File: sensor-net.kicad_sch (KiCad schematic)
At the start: 11 parts

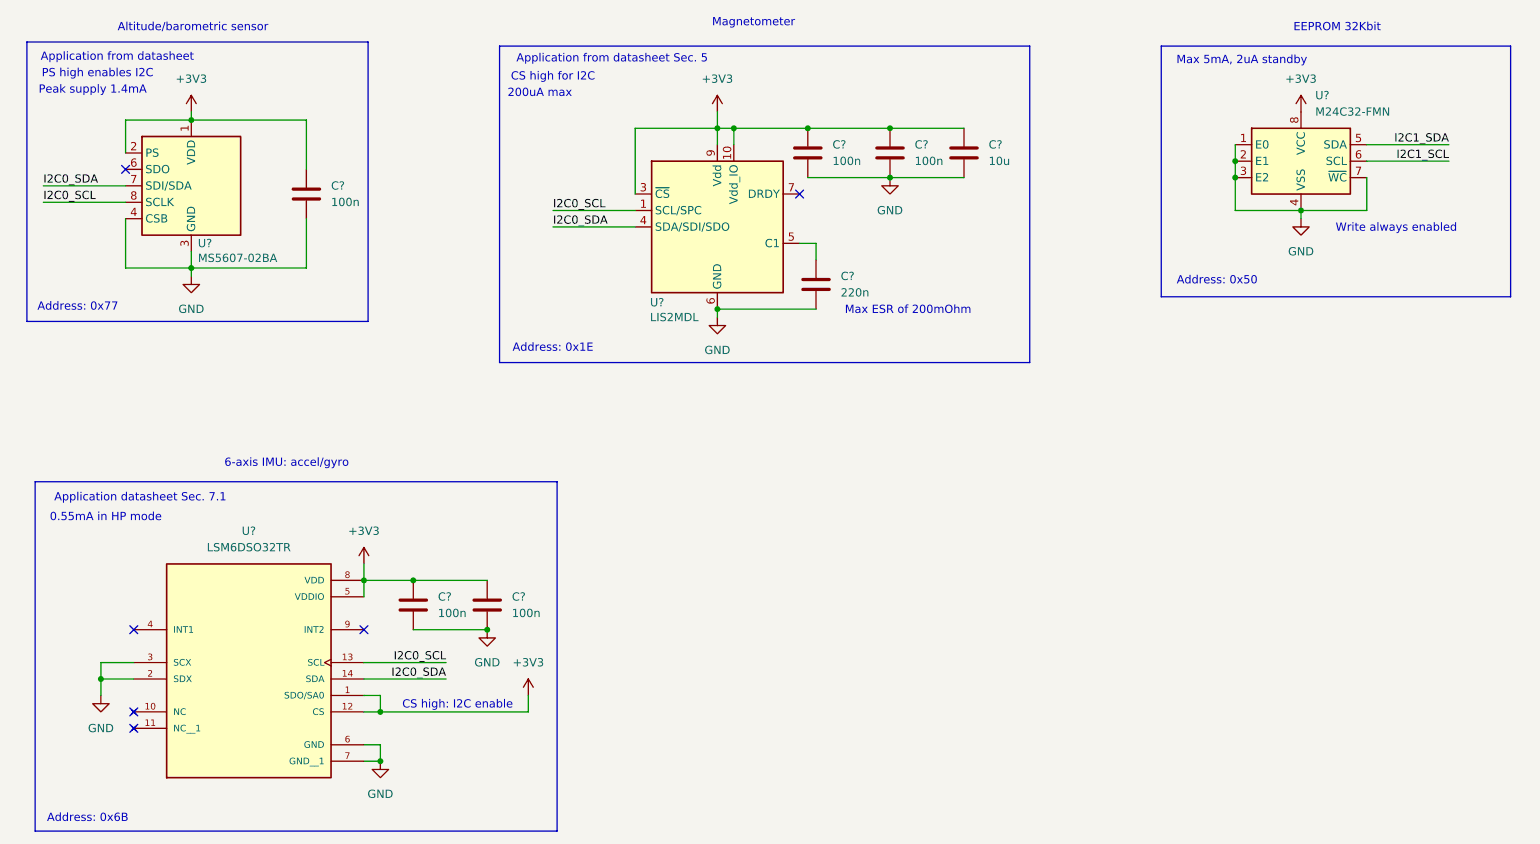
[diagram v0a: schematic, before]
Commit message: Added power circuitry and status LEDs. Went for an LDO with very low dropout voltage to reduce potential noise from a switching reg.
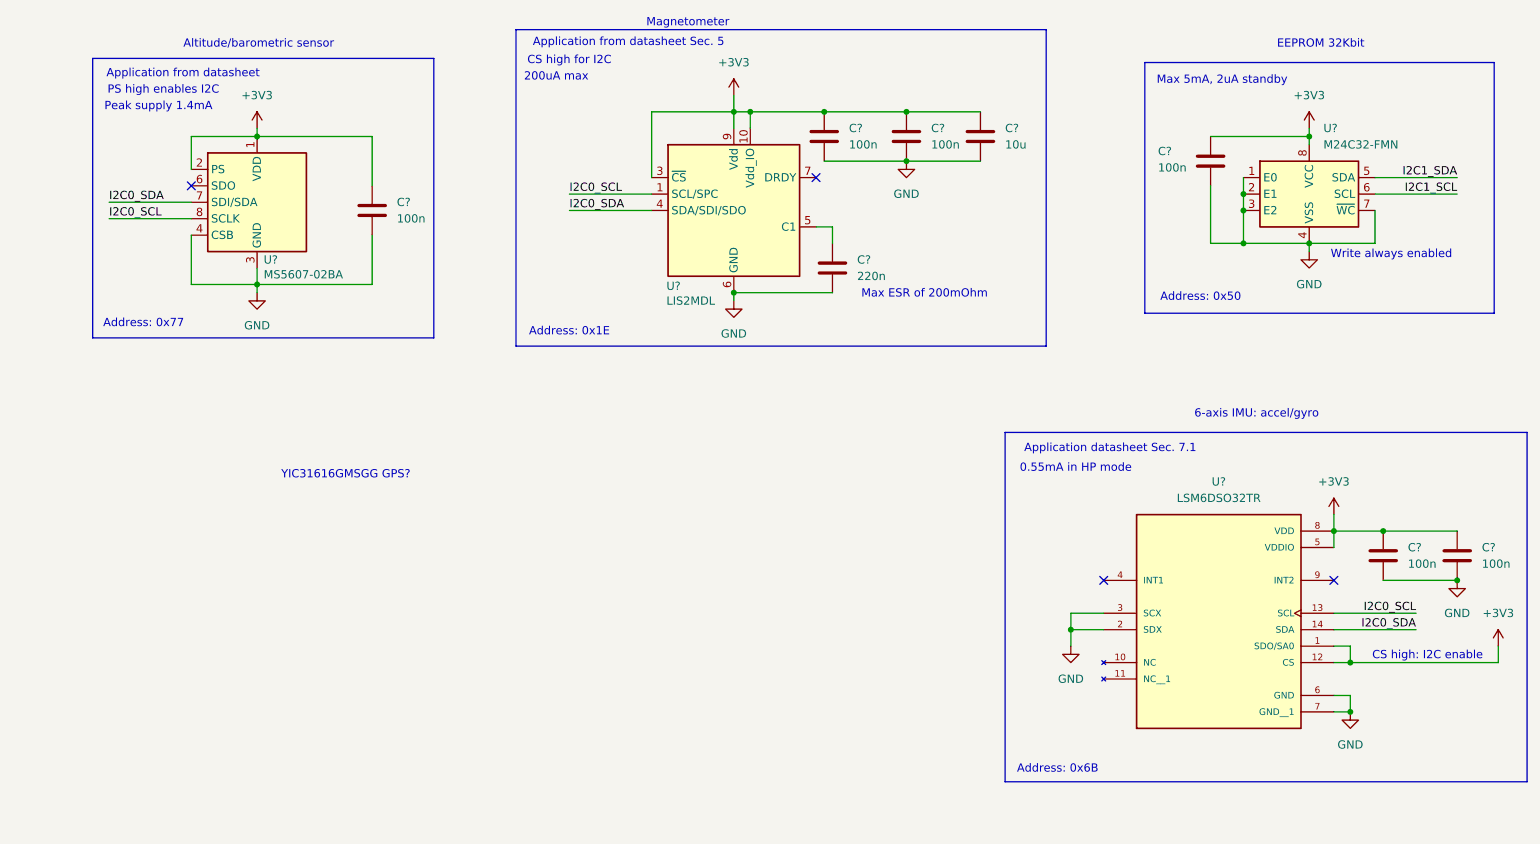
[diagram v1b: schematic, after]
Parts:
- added C?: 100n, symbol Device:C
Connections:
- net +3V3: now also C?.1
- net GND: now also C?.2
- no-connect marks 6 -> 4
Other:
- note added: "YIC31616GMSGG GPS?"
- moved on the sheet: C?, U?

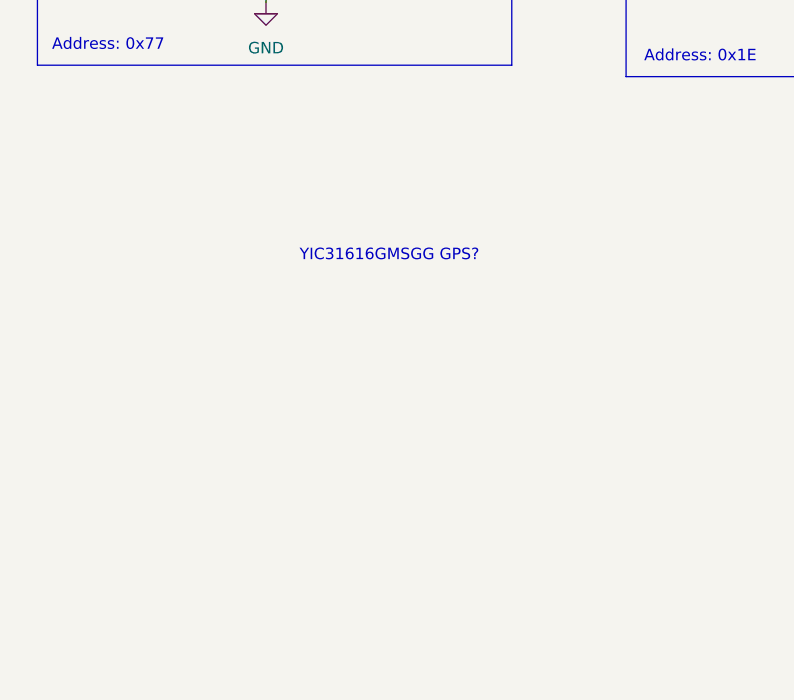
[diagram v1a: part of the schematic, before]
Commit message: Added decoupling caps to RN2483 and fixed antenna connection. Also settled on easy GPS.
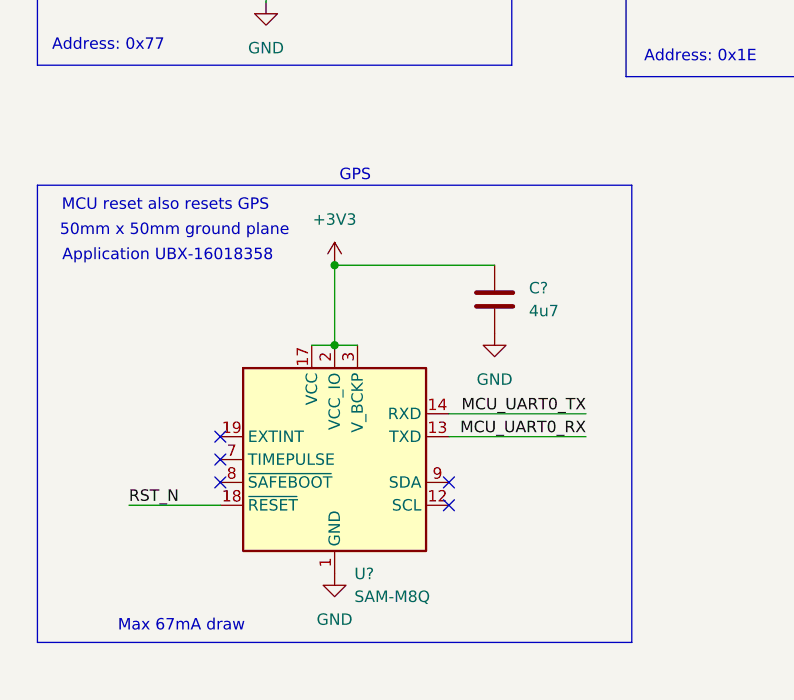
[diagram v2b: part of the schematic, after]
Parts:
- added C?: 4u7, symbol Device:C
- added U?: SAM-M8Q, RF_GPS:ublox_SAM-M8Q, symbol RF_GPS:SAM-M8Q
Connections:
- net +3V3: now also C?.1, U?.17 (VCC), U?.2 (VCC_IO), U?.3 (V_BCKP)
- net GND: now also C?.2, U?.1 (GND), U?.10 (GND), U?.11 (GND), U?.15 (GND), U?.16 (GND), U?.20 (GND), U?.4 (GND), U?.5 (GND), U?.6 (GND)
- new net MCU_UART0_RX: U?.13 (TXD)
- new net MCU_UART0_TX: U?.14 (RXD)
- new net RST_N: U?.18 (~{RESET})
- no-connect marks 4 -> 9
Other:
- note added: "50mm x 50mm ground plane"
- note added: "Application UBX-16018358"
- note added: "GPS"
- note added: "MCU reset also resets GPS"
- note added: "Max 67mA draw"
- note removed: "YIC31616GMSGG GPS?"

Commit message: Updated power supply to use buck regulator and power input MUX. Also computed current draw of the board to size power regulator.
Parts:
- gave numbers to parts that had none: 14

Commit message: Added footprints for all components
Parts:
- C16, C17, C19, C20, C23, C24: footprint (none) -> Capacitor_SMD:C_0201_0603Metric
- C18: footprint (none) -> Capacitor_SMD:C_0805_2012Metric
- C21, C22: footprint (none) -> Capacitor_SMD:C_0603_1608Metric
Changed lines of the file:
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@@
 			)
 		)
-		(property "Footprint" ""
+		(property "Footprint" "Capacitor_SMD:C_0603_1608Metric"
 			(at 153.3652 63.5 0)
 			(effects
@@
 			)
 		)
-		(property "Footprint" ""
+		(property "Footprint" "Capacitor_SMD:C_0201_0603Metric"
 			(at 249.8852 107.95 0)
 			(effects
@@
 			)
 		)
-		(property "Footprint" ""
+		(property "Footprint" "Capacitor_SMD:C_0805_2012Metric"
 			(at 176.2252 43.18 0)
 			(effects
@@
 			)
 		)
-		(property "Footprint" ""
+		(property "Footprint" "Capacitor_SMD:C_0201_0603Metric"
 			(at 164.7952 43.18 0)
 			(effects
@@
 			)
 		)
-		(property "Footprint" ""
+		(property "Footprint" "Capacitor_SMD:C_0201_0603Metric"
 			(at 238.4552 107.95 0)
 			(effects
@@
 			)
 		)
-		(property "Footprint" ""
+		(property "Footprint" "Capacitor_SMD:C_0201_0603Metric"
 			(at 152.0952 43.18 0)
 			(effects
@@
 			)
 		)
-		(property "Footprint" ""
+		(property "Footprint" "Capacitor_SMD:C_0201_0603Metric"
 			(at 82.2452 54.61 0)
 			(effects
@@
 			)
 		)
-		(property "Footprint" ""
+		(property "Footprint" "Capacitor_SMD:C_0603_1608Metric"
 			(at 89.8652 100.33 0)
 			(effects
@@
 			)
 		)
-		(property "Footprint" ""
+		(property "Footprint" "Capacitor_SMD:C_0201_0603Metric"
 			(at 211.7852 46.99 0)
 			(effects
